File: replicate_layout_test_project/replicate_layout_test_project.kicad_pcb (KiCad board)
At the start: 2 copper layers, 70 parts, among them J1001 Pusa_6mm, J1002 Pusa_6mm, J201 Pusa_6mm, J202 Pusa_6mm, J601 Pusa_6mm, J602 Pusa_6mm, Q1101 CSD19531KCS, Q1102 CSD19531KCS, Q1301 CSD19531KCS, Q1302 CSD19531KCS, Q1401 CSD19531KCS, Q1402 CSD19531KCS, Q301 CSD19531KCS, Q302 CSD19531KCS, Q501 CSD19531KCS, Q502 CSD19531KCS, Q701 CSD19531KCS, Q702 CSD19531KCS, Q901 CSD19531KCS, Q902 CSD19531KCS, U101 TMS320F28027DA, U1101 IR2181, U1201 INA240A1D, U1301 IR2181, U1401 IR2181, U301 IR2181, U401 INA240A1D, U501 IR2181, U701 IR2181, U801 INA240A1D, U901 IR2181

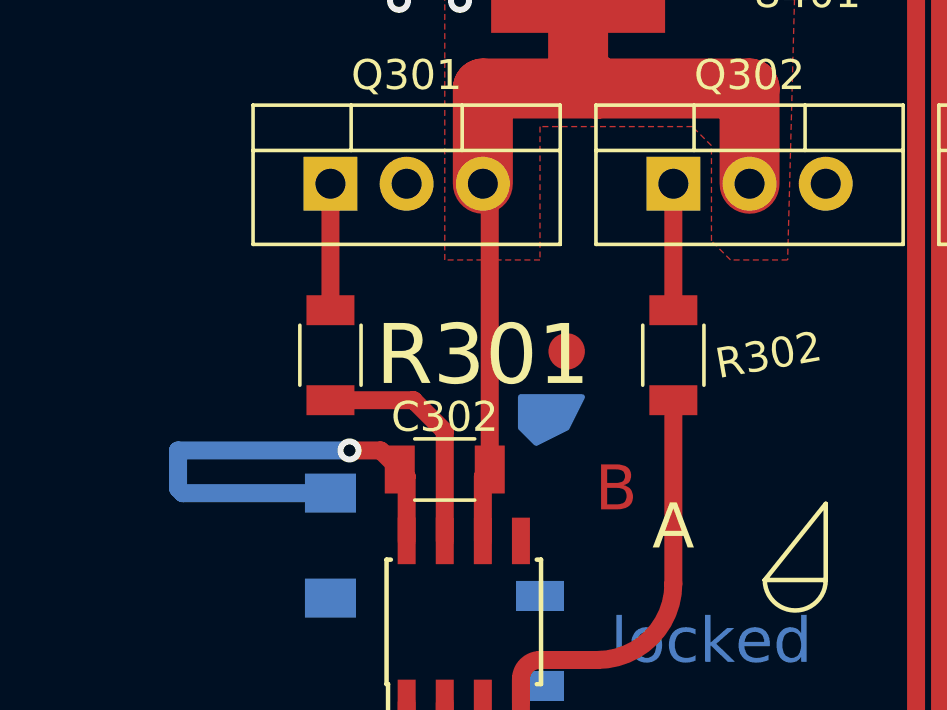
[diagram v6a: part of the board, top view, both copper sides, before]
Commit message: Significant refactoring of item selection code, expand selection to outside sheet items which are within src group
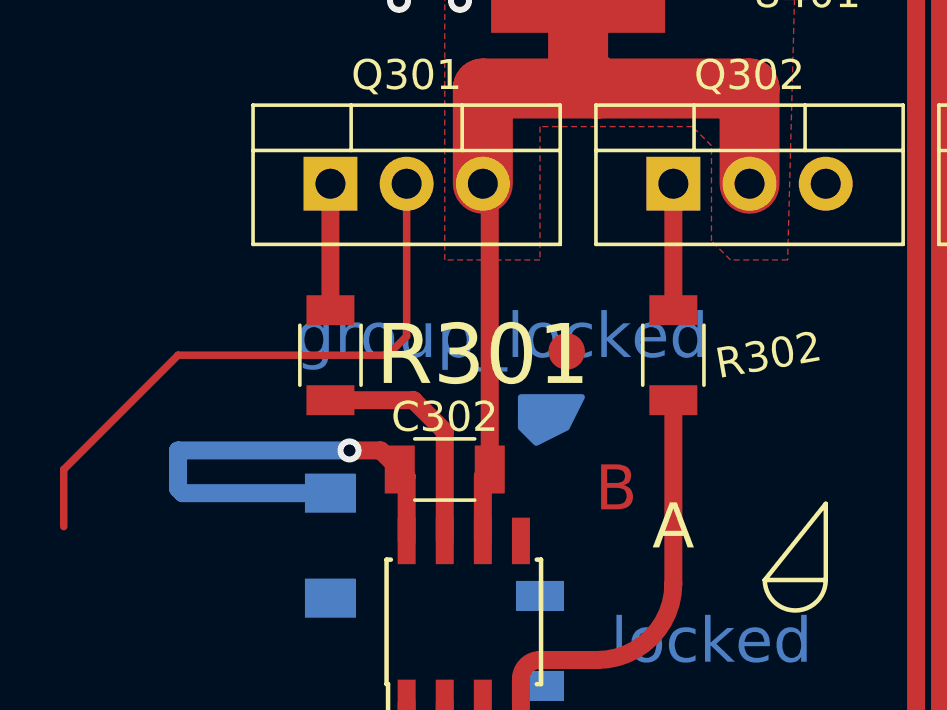
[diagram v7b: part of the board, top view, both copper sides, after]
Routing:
- net +VDC: track 0.00 -> 20.3 mm
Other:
- board text added: "group_locked"
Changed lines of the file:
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@@
+    (effects (font (size 1.5 1.5) (thickness 0.3)))
+  )
+  (gr_text "group_locked" (at 75.565 81.28) (layer "B.Cu")
     (effects (font (size 1.5 1.5) (thickness 0.3)))
   )
@@
   (gr_text "Comment" (at 80.264 85.852) (layer "Cmts.User")
     (effects (font (size 1 1) (thickness 0.15)))
-  )
-  (dimension (type aligned) (layer "Margin")
-    (pts (xy 69.85 81.915) (xy 81.28 81.915))
-    (height -1.6)
-    (gr_text "11,4300 mm" (at 75.565 79.165) (layer "Margin")
-      (effects (font (size 1 1) (thickness 0.15)))
-    )
-    (format (units 3) (units_format 1) (precision 4))
-    (style (thickness 0.15) (arrow_length 1.27) (text_position_mode 0) (extension_height 0.58642) (extension_offset 0.5) keep_text_aligned)
   )
   (dimension (type aligned) (layer "Margin")
@@
     (height -1.6)
     (gr_text "11,4300 mm" (at 98.425 79.165) (layer "Margin")
+      (effects (font (size 1 1) (thickness 0.15)))
+    )
+    (format (units 3) (units_format 1) (precision 4))
+    (style (thickness 0.15) (arrow_length 1.27) (text_position_mode 0) (extension_height 0.58642) (extension_offset 0.5) keep_text_aligned)
+  )
+  (dimension (type aligned) (layer "Margin")
+    (pts (xy 69.85 80.975) (xy 81.28 80.975))
+    (height -1.6)
+    (gr_text "11,4300 mm" (at 75.565 78.225) (layer "Margin")
       (effects (font (size 1 1) (thickness 0.15)))
     )
@@
   (segment (start 78.105 59.77) (end 78.105 50.165) (width 2) (layer "F.Cu") (net 17))
   (segment (start 69.85 80.415) (end 69.85 76.2) (width 0.6) (layer "F.Cu") (net 20))
+  (segment (start 64.77 81.915) (end 60.96 85.725) (width 0.25) (layer "F.Cu") (net 21))
+  (segment (start 72.39 76.2) (end 72.39 81.28) (width 0.25) (layer "F.Cu") (net 21))
+  (segment (start 72.39 81.28) (end 71.755 81.915) (width 0.25) (layer "F.Cu") (net 21))
+  (segment (start 60.96 85.725) (end 60.96 87.63) (width 0.25) (layer "F.Cu") (net 21))
+  (segment (start 71.755 81.915) (end 64.77 81.915) (width 0.25) (layer "F.Cu") (net 21))
   (segment (start 81.28 80.415) (end 81.28 76.2) (width 0.6) (layer "F.Cu") (net 22))
   (segment (start 92.71 80.415) (end 92.71 76.2) (width 0.6) (layer "F.Cu") (net 23))
@@
     (connect_pads yes (clearance 0))
     (min_thickness 0.254)
-    (keepout (tracks not_allowed) (vias not_allowed) (pads not_allowed ) (copperpour allowed) (footprints allowed))
+    (keepout (tracks not_allowed) (vias not_allowed) (pads not_allowed) (copperpour allowed) (footprints allowed))
     (fill (thermal_gap 0.508) (thermal_bridge_width 0.508))
     (polygon
@@
     (connect_pads yes (clearance 0))
     (min_thickness 0.254)
-    (keepout (tracks not_allowed) (vias not_allowed) (pads not_allowed ) (copperpour allowed) (footprints allowed))
+    (keepout (tracks not_allowed) (vias not_allowed) (pads not_allowed) (copperpour allowed) (footprints allowed))
     (fill (thermal_gap 0.508) (thermal_bridge_width 0.508))
     (polygon
@@
     (connect_pads yes (clearance 0))
     (min_thickness 0.254)
-    (keepout (tracks not_allowed) (vias not_allowed) (pads not_allowed ) (copperpour allowed) (footprints allowed))
+    (keepout (tracks not_allowed) (vias not_allowed) (pads not_allowed) (copperpour allowed) (footprints allowed))
     (fill (thermal_gap 0.508) (thermal_bridge_width 0.508))
     (polygon
@@
     (connect_pads yes (clearance 0))
     (min_thickness 0.254)
-    (keepout (tracks not_allowed) (vias not_allowed) (pads not_allowed ) (copperpour allowed) (footprints allowed))
+    (keepout (tracks not_allowed) (vias not_allowed) (pads not_allowed) (copperpour allowed) (footprints allowed))
     (fill (thermal_gap 0.508) (thermal_bridge_width 0.508))
     (polygon
@@
     )
   )
-  (group "room" (id d44b001a-c4b5-4120-9284-6c7991794e28)
+  (group "room" (id 78daec0b-152e-46bf-b1f4-c3f4f2f98fec)
     (members
       078044b2-8672-471f-8af0-713545e8135d
       2c577a47-dd99-484d-98e7-a1a6118d18cf
+      2d0a55a7-119d-4cb1-9161-769d014d9d24
       2fe5489f-7402-4041-8c9c-e18b9abb73fc
+      38031c25-7595-401a-b86b-9e2462e63d8e
+      3896d8e3-13c4-4e01-a766-927ff0202f2b
+      4503bb91-8b1c-4ae7-bc49-f510d40f4b0b
+      482745db-df58-49f7-8fa7-e685d2aac961
       4b91a28b-e778-4691-8d2b-bb09bc10e8e8
+      57017872-efca-4bc3-8148-77c9e40617f4
       71ec2bcf-c838-4d93-88b9-769d3aedab35
+      78697f0e-4a8d-4091-a767-138dce243439
+      80b0765e-da74-4802-9773-9473d0c1ee2a
       813c1703-0564-48c9-a3b7-adb9c37bd3db
+      909af301-8cfe-4457-80b0-d3417bb64680
       90dda447-2750-402e-9a9e-df264b0c0bc9
+      90eccc84-68e3-440b-b8e7-b46a28e3379b
+      98eaf7ef-ce20-4316-b94d-5704f07c1c12
       9ab114d2-6119-40fd-a158-9f9acdc83328
       9ff3d8ce-e8bc-46df-9c01-5053e905e02f
-      adfaccc9-bb80-495a-9038-d58935037d76
+      a6fd658e-c2a8-47e9-8b95-c00e715df72d
+      ae7a8faa-d524-47df-9b3d-5300f09bf258
       b3eebb03-af8c-48e8-a7d9-5ec3741206fa
       b490dd7d-6f2a-4467-a3bc-5bf7d1926b4a
@@
       e28785e6-23a6-4d97-8af1-f33c992f70f8
       e77c19b6-db3d-4b9e-a098-b8ca8297a370
+      e9e24dbe-06a2-4b29-b534-383ad36af2ff
       f587f477-194d-41ae-8a6d-91fbd85f9d3f
     )

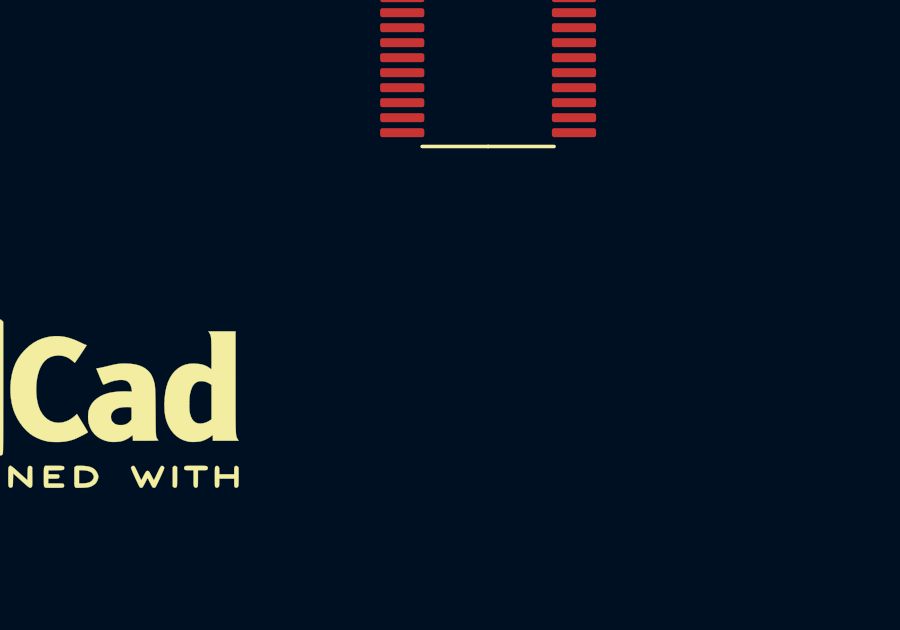
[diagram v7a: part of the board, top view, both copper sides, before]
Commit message: Improve error messages that user sees
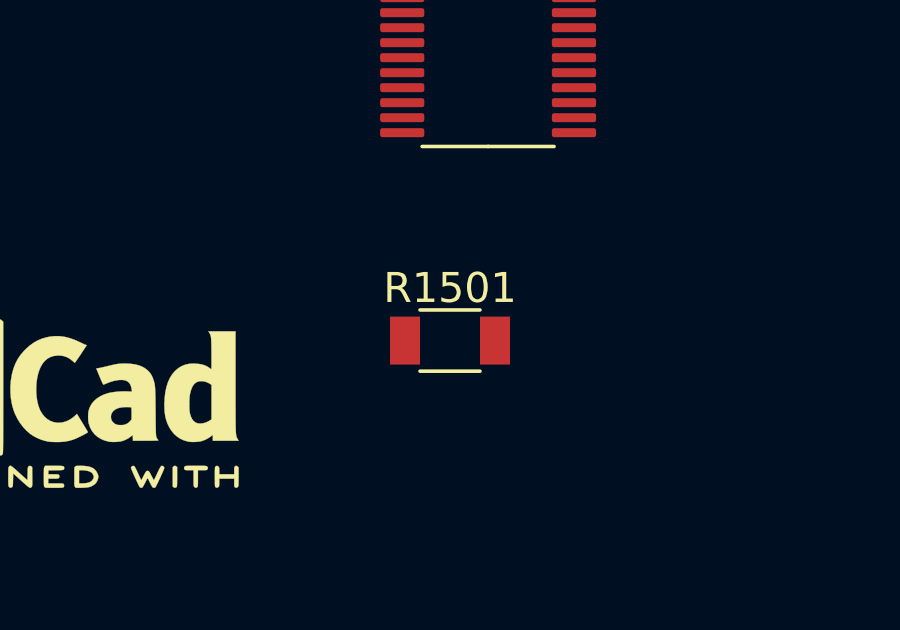
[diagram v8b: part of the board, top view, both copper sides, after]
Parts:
- added R1501: R1206, Passives:R1206M, F.Cu at (95.9, 139.1)
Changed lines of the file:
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@@
   (net 87 "/Full Bridge/Q_high")
   (net 88 "unconnected-(U101-Pad38)")
+  (net 89 "unconnected-(R1501-Pad1)")
+  (net 90 "unconnected-(R1501-Pad2)")
   (footprint "Package_SO:SOIC-8_3.9x4.9mm_P1.27mm" (layer "F.Cu")
     (at 86.36 64.77 90)
@@
       (offset (xyz 0 0 0))
       (scale (xyz 1 1 1))
+      (rotate (xyz 0 0 0))
+    )
+  )
+  (footprint "Passives:R1206M" (layer "F.Cu")
+    (at 95.885 139.065)
+    (descr "Capacitor SMD 1206, reflow soldering, AVX (see smccp.pdf)")
+    (tags "capacitor 1206")
+    (property "Sheetfile" "single.kicad_sch")
+    (property "Sheetname" "single")
+    (attr smd)
+    (fp_text reference "R1501" (at 0 -1.75) (layer "F.SilkS")
+      (effects (font (size 1 1) (thickness 0.15)))
+    )
+    (fp_text value "R1206" (at 0 2) (layer "F.Fab") hide
+      (effects (font (size 1 1) (thickness 0.15)))
+    )
+    (fp_text user "${REFERENCE}" (at 0 0) (layer "F.Fab")
+      (effects (font (size 0.5 0.5) (thickness 0.07)))
+    )
+    (fp_line (start -1 1.02) (end 1 1.02) (layer "F.SilkS") (width 0.12))
+    (fp_line (start 1 -1.02) (end -1 -1.02) (layer "F.SilkS") (width 0.12))
+    (fp_line (start -2.25 -1.05) (end 2.25 -1.05) (layer "F.CrtYd") (width 0.05))
+    (fp_line (start 2.25 1.05) (end -2.25 1.05) (layer "F.CrtYd") (width 0.05))
+    (fp_line (start -2.25 -1.05) (end -2.25 1.05) (layer "F.CrtYd") (width 0.05))
+    (fp_line (start 2.25 1.05) (end 2.25 -1.05) (layer "F.CrtYd") (width 0.05))
+    (fp_line (start 1.6 0.8) (end -1.6 0.8) (layer "F.Fab") (width 0.1))
+    (fp_line (start 1.6 -0.8) (end 1.6 0.8) (layer "F.Fab") (width 0.1))
+    (fp_line (start -1.6 0.8) (end -1.6 -0.8) (layer "F.Fab") (width 0.1))
+    (fp_line (start -1.6 -0.8) (end 1.6 -0.8) (layer "F.Fab") (width 0.1))
+    (pad "1" smd rect locked (at -1.5 0) (size 1 1.6) (layers "F.Cu" "F.Paste" "F.Mask")
+      (net 89 "unconnected-(R1501-Pad1)") (pintype "passive"))
+    (pad "2" smd rect locked (at 1.5 0) (size 1 1.6) (layers "F.Cu" "F.Paste" "F.Mask")
+      (net 90 "unconnected-(R1501-Pad2)") (pintype "passive"))
+    (model "${KICAD6_3DMODEL_DIR}/Resistor_SMD.3dshapes/R_1206_3216Metric.wrl"
+      (offset (xyz 0 0 0))
+      (scale (xyz 1 1 1))
